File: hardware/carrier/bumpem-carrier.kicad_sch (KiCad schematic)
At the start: 22 parts, among them J1 Module A, J2 Module B, J3 Module C, J4 Module D, U1 Teensy 4.1, U2 MCP4728 (Adafruit 4470)

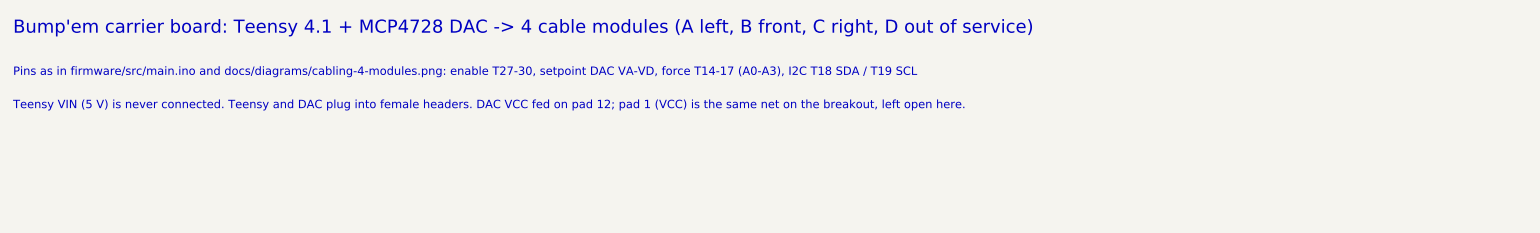
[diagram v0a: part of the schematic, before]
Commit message: docs: carrier board spacing (force tracks clear of socket pins, gaps >= 0.74 mm), module D active
Co-Authored-By: Claude Opus 5.5 <noreply@anthropic.com>
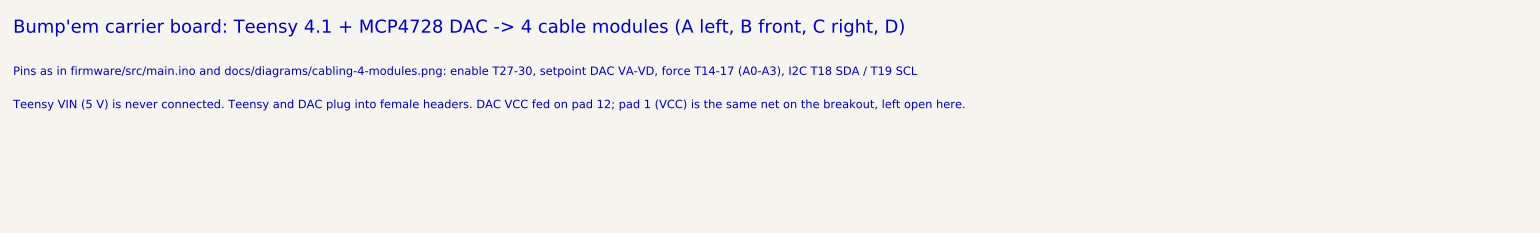
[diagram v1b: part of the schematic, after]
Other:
- note added: "Bump'em carrier board: Teensy 4.1 + MCP4728 DAC -> 4 cable modules (A left, B front, C right, D)"
- note removed: "Bump'em carrier board: Teensy 4.1 + MCP4728 DAC -> 4 cable modules (A left, B front, C right, D out of service)"
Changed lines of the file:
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@@
   (instances (project "bumpem-carrier" (path "/59954970-40fd-5ce1-8984-f1894c2a73a3" (reference "H4") (unit 1))))
 )
-(text "Bump'em carrier board: Teensy 4.1 + MCP4728 DAC -> 4 cable modules (A left, B front, C right, D out of service)" (exclude_from_sim no) (at 20.32 20.32 0) (effects (font (size 2.0 2.0)) (justify left bottom)))
+(text "Bump'em carrier board: Teensy 4.1 + MCP4728 DAC -> 4 cable modules (A left, B front, C right, D)" (exclude_from_sim no) (at 20.32 20.32 0) (effects (font (size 2.0 2.0)) (justify left bottom)))
 (text "Pins as in firmware/src/main.ino and docs/diagrams/cabling-4-modules.png: enable T27-30, setpoint DAC VA-VD, force T14-17 (A0-A3), I2C T18 SDA / T19 SCL" (exclude_from_sim no) (at 20.32 26.67 0) (effects (font (size 1.27 1.27)) (justify left bottom)))
 (text "Teensy VIN (5 V) is never connected. Teensy and DAC plug into female headers. DAC VCC fed on pad 12; pad 1 (VCC) is the same net on the breakout, left open here." (exclude_from_sim no) (at 20.32 31.75 0) (effects (font (size 1.27 1.27)) (justify left bottom)))

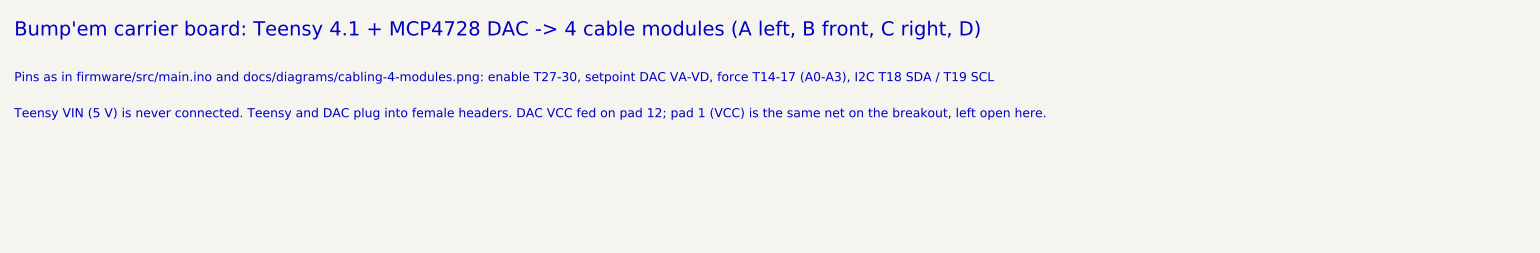
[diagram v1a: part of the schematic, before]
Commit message: api: perturbation by angle (Vicon axes, split over neighbouring cables), geometry endpoint, bumpem perturb; module D back
Co-Authored-By: Claude Opus 5.5 <noreply@anthropic.com>
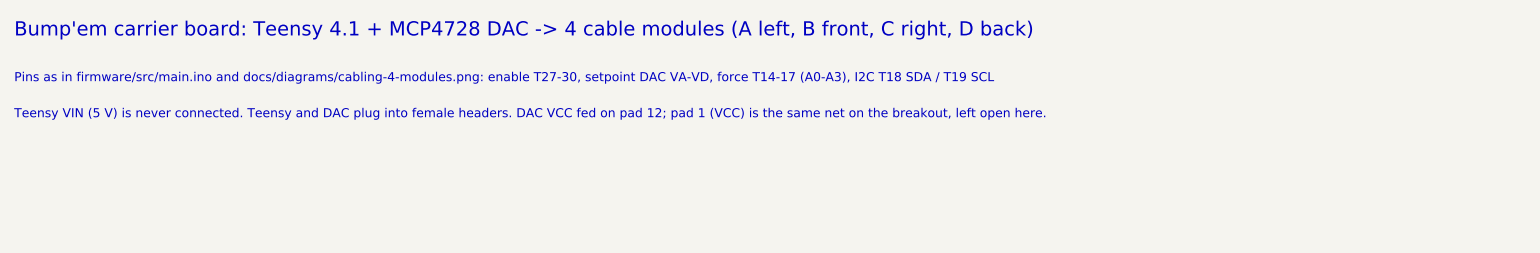
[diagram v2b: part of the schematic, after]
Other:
- note added: "Bump'em carrier board: Teensy 4.1 + MCP4728 DAC -> 4 cable modules (A left, B front, C right, D back)"
- note removed: "Bump'em carrier board: Teensy 4.1 + MCP4728 DAC -> 4 cable modules (A left, B front, C right, D)"
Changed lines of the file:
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@@
   (instances (project "bumpem-carrier" (path "/59954970-40fd-5ce1-8984-f1894c2a73a3" (reference "H4") (unit 1))))
 )
-(text "Bump'em carrier board: Teensy 4.1 + MCP4728 DAC -> 4 cable modules (A left, B front, C right, D)" (exclude_from_sim no) (at 20.32 20.32 0) (effects (font (size 2.0 2.0)) (justify left bottom)))
+(text "Bump'em carrier board: Teensy 4.1 + MCP4728 DAC -> 4 cable modules (A left, B front, C right, D back)" (exclude_from_sim no) (at 20.32 20.32 0) (effects (font (size 2.0 2.0)) (justify left bottom)))
 (text "Pins as in firmware/src/main.ino and docs/diagrams/cabling-4-modules.png: enable T27-30, setpoint DAC VA-VD, force T14-17 (A0-A3), I2C T18 SDA / T19 SCL" (exclude_from_sim no) (at 20.32 26.67 0) (effects (font (size 1.27 1.27)) (justify left bottom)))
 (text "Teensy VIN (5 V) is never connected. Teensy and DAC plug into female headers. DAC VCC fed on pad 12; pad 1 (VCC) is the same net on the breakout, left open here." (exclude_from_sim no) (at 20.32 31.75 0) (effects (font (size 1.27 1.27)) (justify left bottom)))

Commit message: docs: carrier board pluggable module connectors (Phoenix MSTB 2,5 with flanges), board 154 x 96 mm
Co-Authored-By: Claude Opus 5.5 <noreply@anthropic.com>
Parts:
- J1, J2, J3, J4: footprint TerminalBlock_Phoenix:TerminalBlock_Phoenix_MKDS-1,5-5-5.08_1x05_P5.08mm_Horizontal -> Connector_Phoenix_MSTB:PhoenixContact_MSTB_2,5_5-GF-5,08_1x05_P5.08mm_Horizontal_ThreadedFlange
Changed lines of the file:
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@@
   (property "Reference" "J1" (at 388.62 49.53 0) (effects (font (size 1.27 1.27)) (justify left)))
   (property "Value" "Module A" (at 388.62 58.42 0) (effects (font (size 1.27 1.27)) (justify left)))
-  (property "Footprint" "TerminalBlock_Phoenix:TerminalBlock_Phoenix_MKDS-1,5-5-5.08_1x05_P5.08mm_Horizontal" (at 386.08 50.80 0) (effects (font (size 1.27 1.27)) hide))
+  (property "Footprint" "Connector_Phoenix_MSTB:PhoenixContact_MSTB_2,5_5-GF-5,08_1x05_P5.08mm_Horizontal_ThreadedFlange" (at 386.08 50.80 0) (effects (font (size 1.27 1.27)) hide))
   (property "Datasheet" "~" (at 386.08 50.80 0) (effects (font (size 1.27 1.27)) hide))
   (property "Description" "" (at 386.08 50.80 0) (effects (font (size 1.27 1.27)) hide))
@@
   (property "Reference" "J2" (at 388.62 106.68 0) (effects (font (size 1.27 1.27)) (justify left)))
   (property "Value" "Module B" (at 388.62 115.57 0) (effects (font (size 1.27 1.27)) (justify left)))
-  (property "Footprint" "TerminalBlock_Phoenix:TerminalBlock_Phoenix_MKDS-1,5-5-5.08_1x05_P5.08mm_Horizontal" (at 386.08 107.95 0) (effects (font (size 1.27 1.27)) hide))
+  (property "Footprint" "Connector_Phoenix_MSTB:PhoenixContact_MSTB_2,5_5-GF-5,08_1x05_P5.08mm_Horizontal_ThreadedFlange" (at 386.08 107.95 0) (effects (font (size 1.27 1.27)) hide))
   (property "Datasheet" "~" (at 386.08 107.95 0) (effects (font (size 1.27 1.27)) hide))
   (property "Description" "" (at 386.08 107.95 0) (effects (font (size 1.27 1.27)) hide))
@@
   (property "Reference" "J3" (at 388.62 163.83 0) (effects (font (size 1.27 1.27)) (justify left)))
   (property "Value" "Module C" (at 388.62 172.72 0) (effects (font (size 1.27 1.27)) (justify left)))
-  (property "Footprint" "TerminalBlock_Phoenix:TerminalBlock_Phoenix_MKDS-1,5-5-5.08_1x05_P5.08mm_Horizontal" (at 386.08 165.10 0) (effects (font (size 1.27 1.27)) hide))
+  (property "Footprint" "Connector_Phoenix_MSTB:PhoenixContact_MSTB_2,5_5-GF-5,08_1x05_P5.08mm_Horizontal_ThreadedFlange" (at 386.08 165.10 0) (effects (font (size 1.27 1.27)) hide))
   (property "Datasheet" "~" (at 386.08 165.10 0) (effects (font (size 1.27 1.27)) hide))
   (property "Description" "" (at 386.08 165.10 0) (effects (font (size 1.27 1.27)) hide))
@@
   (property "Reference" "J4" (at 388.62 220.98 0) (effects (font (size 1.27 1.27)) (justify left)))
   (property "Value" "Module D" (at 388.62 229.87 0) (effects (font (size 1.27 1.27)) (justify left)))
-  (property "Footprint" "TerminalBlock_Phoenix:TerminalBlock_Phoenix_MKDS-1,5-5-5.08_1x05_P5.08mm_Horizontal" (at 386.08 222.25 0) (effects (font (size 1.27 1.27)) hide))
+  (property "Footprint" "Connector_Phoenix_MSTB:PhoenixContact_MSTB_2,5_5-GF-5,08_1x05_P5.08mm_Horizontal_ThreadedFlange" (at 386.08 222.25 0) (effects (font (size 1.27 1.27)) hide))
   (property "Datasheet" "~" (at 386.08 222.25 0) (effects (font (size 1.27 1.27)) hide))
   (property "Description" "" (at 386.08 222.25 0) (effects (font (size 1.27 1.27)) hide))
